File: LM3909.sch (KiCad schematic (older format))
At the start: 18 parts, among them Q1 BC847, Q2A1 BC807, Q2B1 BC807, Q3 BC847, Q4 BC847

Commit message: add pins to schematic
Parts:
- added J? (x2): Conn_01x04, symbol Conn_01x04
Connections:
- net at BT1.1 (+), Q2A1.2 (E), Q2B1.2 (E)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: now also J?.1 (Pin_1)
- net at D1.2 (A), R1.2: now also J?.2 (Pin_2)
- net at C1.1, Q3.3 (C), R5.2: now also J?.2 (Pin_2)
- net at C1.2, D1.1 (K), R2.1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: now also J?.4 (Pin_4)
- net at BT1.2 (-), Q3.2 (E), R3.2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: now also J?.4 (Pin_4)
- net at R2.2, R3.1: now also J?.1 (Pin_1)
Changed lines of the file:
@@
 	5650 1500 6050 1500
+Wire Wire Line
+	6050 1500 6400 1500
 Wire Wire Line
 	3000 1500 3000 1600
@@
 	3000 1950 3000 2000
 Wire Wire Line
-	2400 1900 2400 2000
+	2400 1900 2400 1950
+Wire Wire Line
+	2400 1950 2400 2000
 Wire Wire Line
 	2400 2300 2400 2400
 Wire Wire Line
-	2400 2400 2400 3050
+	2400 2400 2400 2500
+Wire Wire Line
+	2400 2500 2400 3050
 Wire Wire Line
 	2400 3050 2400 3200
@@
 	3000 2300 3000 2400
 Wire Wire Line
-	3000 2400 3000 3150
+	3000 2400 3000 2650
+Wire Wire Line
+	3000 2650 3000 3150
 Wire Wire Line
 	3000 1950 3400 1950
@@
 Connection ~ 2400 3050
 Wire Wire Line
-	2400 3500 2400 3600
+	2400 3500 2400 3550
+Wire Wire Line
+	2400 3550 2400 3600
 Wire Wire Line
 	2400 3900 2400 4000
+Wire Wire Line
+	1800 4000 2400 4000
 Wire Wire Line
 	2400 4000 3000 4000
@@
 	5650 3350 5650 3050
 Wire Wire Line
-	4750 2250 4750 2150
+	4750 2050 4750 2150
 Wire Wire Line
-	4750 2150 4750 2050
+	4750 2150 4750 2250
 Wire Wire Line
 	5200 2150 4750 2150
 Connection ~ 4750 2150
+$Comp
+L Conn_01x04 J?
+U 1 1 5A21951D
+P 6950 2400
+F 0 "J?" H 6950 2600 50  0000 C CNN
+F 1 "Conn_01x04" H 6950 2100 50  0000 C CNN
+F 2 "" H 6950 2400 50  0001 C CNN
+F 3 "" H 6950 2400 50  0001 C CNN
+	1    6950 2400
+	1    0    0    1
+$EndComp
+$Comp
+L Conn_01x04 J?
+U 1 1 5A21958D
+P 1500 2200
+F 0 "J?" H 1500 2400 50  0000 C CNN
+F 1 "Conn_01x04" H 1500 1900 50  0000 C CNN
+F 2 "" H 1500 2200 50  0001 C CNN
+F 3 "" H 1500 2200 50  0001 C CNN
+	1    1500 2200
+	-1   0    0    -1
+$EndComp
+Wire Wire Line
+	1700 2100 2100 2100
+Wire Wire Line
+	2100 2100 2100 3550
+Wire Wire Line
+	2100 3550 2400 3550
+Connection ~ 2400 3550
+Wire Wire Line
+	1700 2200 1950 2200
+Wire Wire Line
+	1950 2200 1950 2650
+Wire Wire Line
+	1950 2650 3000 2650
+Connection ~ 3000 2650
+Wire Wire Line
+	1700 2400 1800 2400
+Wire Wire Line
+	1800 2400 1800 4000
+Connection ~ 2400 4000
+Wire Wire Line
+	6750 2500 6400 2500
+Wire Wire Line
+	6400 2500 6400 1500
+Connection ~ 6050 1500
+Wire Wire Line
+	6750 2200 6650 2200
+Wire Wire Line
+	6650 2200 6650 4100
+Wire Wire Line
+	6650 4100 2250 4100
+Wire Wire Line
+	2250 4100 2250 2500
+Wire Wire Line
+	2250 2500 2400 2500
+Connection ~ 2400 2500
+Wire Wire Line
+	6750 2400 6500 2400
+Wire Wire Line
+	6500 2400 6500 1300
+Wire Wire Line
+	6500 1300 2200 1300
+Wire Wire Line
+	2200 1300 2200 1950
+Wire Wire Line
+	2200 1950 2400 1950
+Connection ~ 2400 1950
 $EndSCHEMATC

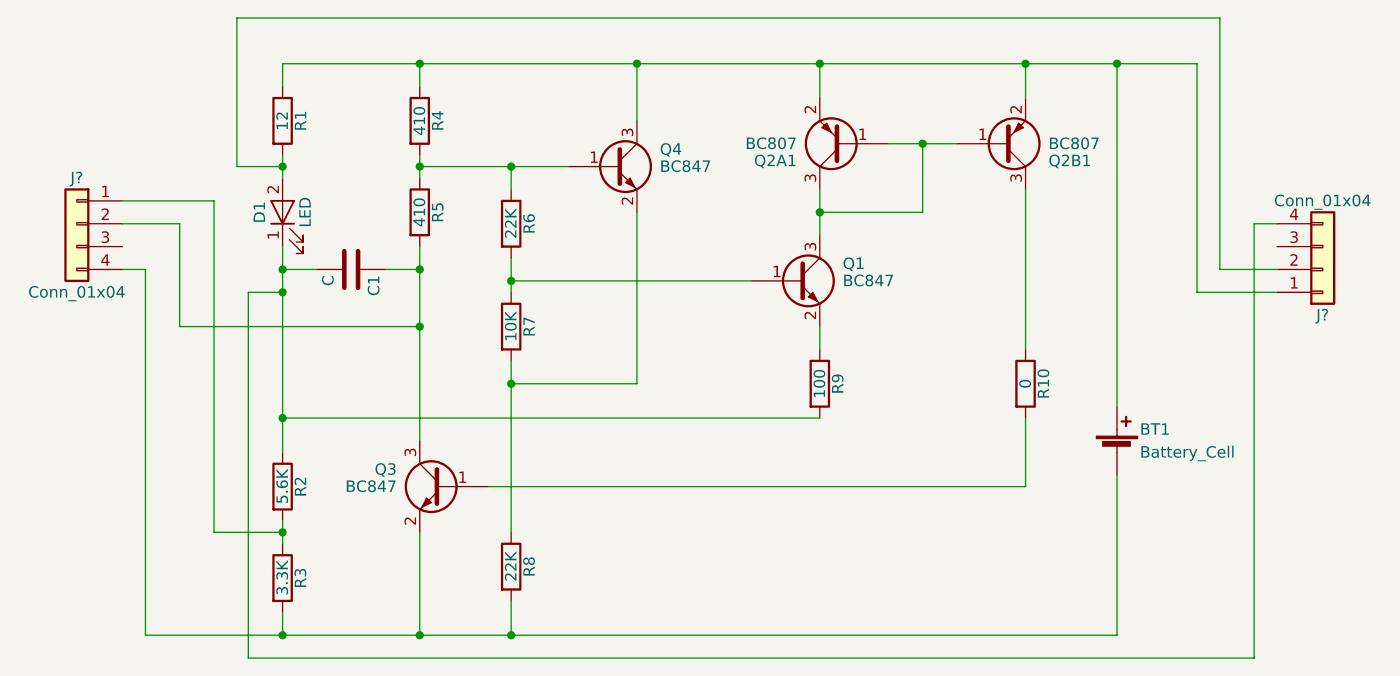
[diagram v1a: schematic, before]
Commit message: add through hole pin footprint
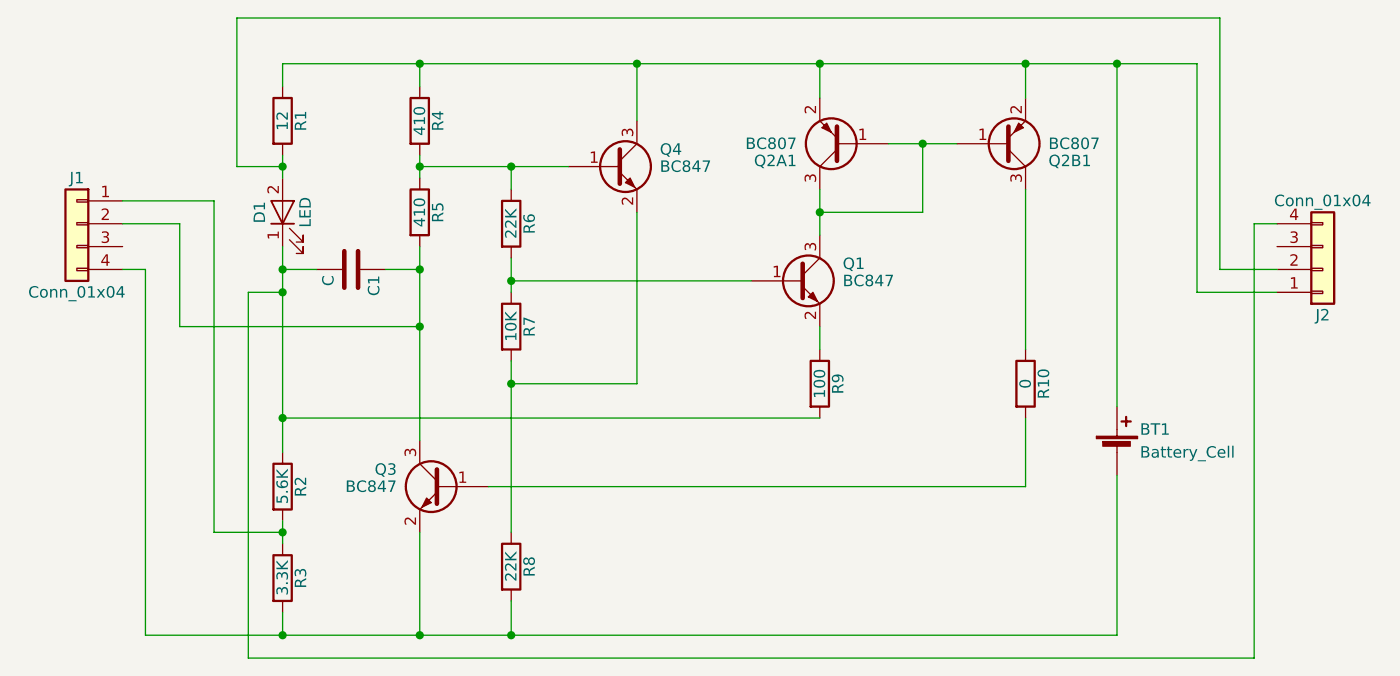
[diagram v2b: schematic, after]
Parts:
- J1, J2: renamed from J?; footprint (none) -> Pin_Headers:Pin_Header_Straight_1x04_Pitch2.54mm
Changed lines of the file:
@@
 	2400 1500 2400 1600
 Wire Wire Line
-	2400 1500 3000 1500
-Wire Wire Line
-	3000 1500 3950 1500
-Wire Wire Line
-	3950 1500 4750 1500
-Wire Wire Line
-	4750 1500 5650 1500
-Wire Wire Line
-	5650 1500 6050 1500
-Wire Wire Line
-	6050 1500 6400 1500
+	2400 1500 6400 1500
 Wire Wire Line
 	3000 1500 3000 1600
 Wire Wire Line
-	3000 1900 3000 1950
+	3000 1900 3000 2000
 Wire Wire Line
-	3000 1950 3000 2000
+	2400 1900 2400 2000
 Wire Wire Line
-	2400 1900 2400 1950
-Wire Wire Line
-	2400 1950 2400 2000
-Wire Wire Line
-	2400 2300 2400 2400
-Wire Wire Line
-	2400 2400 2400 2500
-Wire Wire Line
-	2400 2500 2400 3050
-Wire Wire Line
-	2400 3050 2400 3200
+	2400 2300 2400 3200
 Wire Wire Line
 	2400 2400 2550 2400
@@
 	2850 2400 3000 2400
 Wire Wire Line
-	3000 2300 3000 2400
+	3000 2300 3000 3150
 Wire Wire Line
-	3000 2400 3000 2650
-Wire Wire Line
-	3000 2650 3000 3150
-Wire Wire Line
-	3000 1950 3400 1950
-Wire Wire Line
-	3400 1950 3650 1950
+	3000 1950 3650 1950
 Connection ~ 3000 1950
 Wire Wire Line
@@
 Connection ~ 3400 1950
 Wire Wire Line
-	3400 2350 3400 2450
+	3400 2350 3400 2500
 Wire Wire Line
-	3400 2450 3400 2500
-Wire Wire Line
-	3400 2800 3400 2900
-Wire Wire Line
-	3400 2900 3400 3550
+	3400 2800 3400 3550
 Wire Wire Line
 	3400 2900 3950 2900
@@
 Connection ~ 2400 3050
 Wire Wire Line
-	2400 3500 2400 3550
-Wire Wire Line
-	2400 3550 2400 3600
+	2400 3500 2400 3600
 Wire Wire Line
 	2400 3900 2400 4000
 Wire Wire Line
-	1800 4000 2400 4000
-Wire Wire Line
-	2400 4000 3000 4000
-Wire Wire Line
-	3000 4000 3400 4000
-Wire Wire Line
-	3400 4000 6050 4000
+	1800 4000 6050 4000
 Wire Wire Line
 	3000 4000 3000 3550
@@
 Connection ~ 3400 2900
 Wire Wire Line
-	5050 1850 5200 1850
-Wire Wire Line
-	5200 1850 5350 1850
+	5050 1850 5350 1850
 Wire Wire Line
 	3950 1500 3950 1750
@@
 	5650 3350 5650 3050
 Wire Wire Line
-	4750 2050 4750 2150
-Wire Wire Line
-	4750 2150 4750 2250
+	4750 2050 4750 2250
 Wire Wire Line
 	5200 2150 4750 2150
 Connection ~ 4750 2150
 $Comp
-L Conn_01x04 J?
+L Conn_01x04 J2
 U 1 1 5A21951D
 P 6950 2400
-F 0 "J?" H 6950 2600 50  0000 C CNN
+F 0 "J2" H 6950 2600 50  0000 C CNN
 F 1 "Conn_01x04" H 6950 2100 50  0000 C CNN
-F 2 "" H 6950 2400 50  0001 C CNN
+F 2 "Pin_Headers:Pin_Header_Straight_1x04_Pitch2.54mm" H 6950 2400 50  0001 C CNN
 F 3 "" H 6950 2400 50  0001 C CNN
 	1    6950 2400
@@
 $EndComp
 $Comp
-L Conn_01x04 J?
+L Conn_01x04 J1
 U 1 1 5A21958D
 P 1500 2200
-F 0 "J?" H 1500 2400 50  0000 C CNN
+F 0 "J1" H 1500 2400 50  0000 C CNN
 F 1 "Conn_01x04" H 1500 1900 50  0000 C CNN
-F 2 "" H 1500 2200 50  0001 C CNN
+F 2 "Pin_Headers:Pin_Header_Straight_1x04_Pitch2.54mm" H 1500 2200 50  0001 C CNN
 F 3 "" H 1500 2200 50  0001 C CNN
 	1    1500 2200

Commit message: replace BC8*7 with MMBT390* transistors
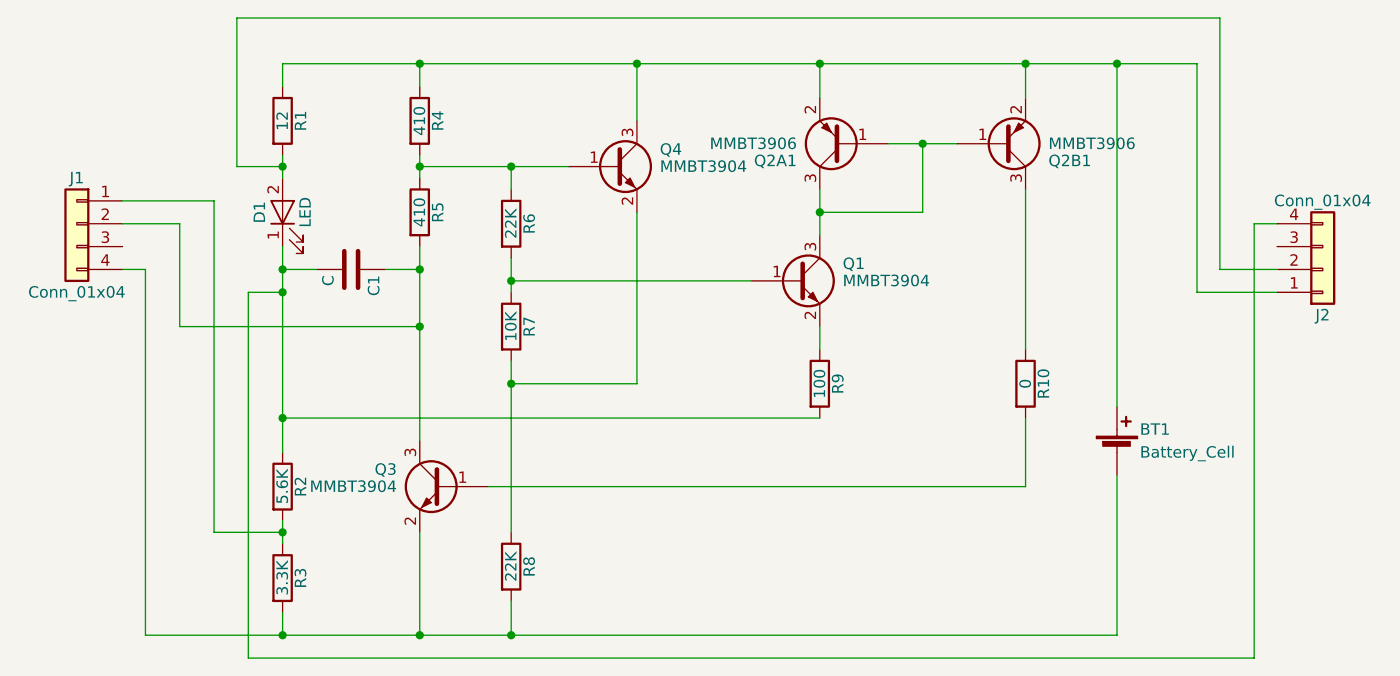
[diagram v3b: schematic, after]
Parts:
- removed Q1, Q3, Q4: BC847, TO_SOT_Packages_SMD:SOT-23, symbol BC847
- removed Q2A1, Q2B1: BC807, TO_SOT_Packages_SMD:SOT-23, symbol BC807
- added Q1, Q3, Q4: MMBT3904, TO_SOT_Packages_SMD:SOT-23, symbol MMBT3904
- added Q2A1, Q2B1: MMBT3906, TO_SOT_Packages_SMD:SOT-23, symbol MMBT3906
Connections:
- net at BT1.1 (+), J2.1 (Pin_1), R1.1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: now also Q2A1.2 (E), Q2B1.2 (E), Q4.3 (C)
- net at R4.2, R5.1, R6.1: now also Q4.1 (B)
- net at C1.1, J1.2 (Pin_2), R5.2: now also Q3.3 (C)
- net at R9.1: now also Q1.2 (E)
- net at R7.2, R8.1: now also Q4.2 (E)
- net at BT1.2 (-), J1.4 (Pin_4), R3.2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: now also Q3.2 (E)
- net at R6.2, R7.1: now also Q1.1 (B)
- net at R10.2: now also Q3.1 (B)
- net at R10.1: now also Q2B1.3 (C)
- new net: Q1.3 (C), Q2A1.1 (B), Q2A1.3 (C), Q2B1.1 (B)
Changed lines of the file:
@@
-$EndComp
-$Comp
-L BC847 Q4
-U 1 1 5A204D01
-P 3850 1950
-F 0 "Q4" H 4050 2025 50  0000 L CNN
-F 1 "BC847" H 4050 1950 50  0000 L CNN
-F 2 "TO_SOT_Packages_SMD:SOT-23" H 4050 1875 50  0001 L CIN
-F 3 "" H 3850 1950 50  0001 L CNN
-	1    3850 1950
-	1    0    0    -1
-$EndComp
-$Comp
-L BC847 Q1
-U 1 1 5A2054C7
-P 4650 2450
-F 0 "Q1" H 4850 2525 50  0000 L CNN
-F 1 "BC847" H 4850 2450 50  0000 L CNN
-F 2 "TO_SOT_Packages_SMD:SOT-23" H 4850 2375 50  0001 L CIN
-F 3 "" H 4650 2450 50  0001 L CNN
-	1    4650 2450
-	1    0    0    -1
-$EndComp
-$Comp
-L BC847 Q3
-U 1 1 5A205527
-P 3100 3350
-F 0 "Q3" H 3300 3425 50  0000 L CNN
-F 1 "BC847" H 3300 3350 50  0000 L CNN
-F 2 "TO_SOT_Packages_SMD:SOT-23" H 3300 3275 50  0001 L CIN
-F 3 "" H 3100 3350 50  0001 L CNN
-	1    3100 3350
-	-1   0    0    -1
-$EndComp
-$Comp
-L BC807 Q2B1
-U 1 1 5A205CDD
-P 5550 1850
-F 0 "Q2B1" H 5750 1925 50  0000 L CNN
-F 1 "BC807" H 5750 1850 50  0000 L CNN
-F 2 "TO_SOT_Packages_SMD:SOT-23" H 5750 1775 50  0001 L CIN
-F 3 "" H 5550 1850 50  0001 L CNN
-	1    5550 1850
-	1    0    0    1
-$EndComp
-$Comp
-L BC807 Q2A1
-U 1 1 5A205D5E
-P 4850 1850
-F 0 "Q2A1" H 5050 1925 50  0000 L CNN
-F 1 "BC807" H 5050 1850 50  0000 L CNN
-F 2 "TO_SOT_Packages_SMD:SOT-23" H 5050 1775 50  0001 L CIN
-F 3 "" H 4850 1850 50  0001 L CNN
-	1    4850 1850
-	-1   0    0    1
 $EndComp
 $Comp
@@
 	2200 1950 2400 1950
 Connection ~ 2400 1950
+$Comp
+L MMBT3904 Q4
+U 1 1 5A256999
+P 3850 1950
+F 0 "Q4" H 4050 2025 50  0000 L CNN
+F 1 "MMBT3904" H 4050 1950 50  0000 L CNN
+F 2 "TO_SOT_Packages_SMD:SOT-23" H 4050 1875 50  0001 L CIN
+F 3 "" H 3850 1950 50  0001 L CNN
+	1    3850 1950
+	1    0    0    -1
+$EndComp
+$Comp
+L MMBT3904 Q1
+U 1 1 5A256DC3
+P 4650 2450
+F 0 "Q1" H 4850 2525 50  0000 L CNN
+F 1 "MMBT3904" H 4850 2450 50  0000 L CNN
+F 2 "TO_SOT_Packages_SMD:SOT-23" H 4850 2375 50  0001 L CIN
+F 3 "" H 4650 2450 50  0001 L CNN
+	1    4650 2450
+	1    0    0    -1
+$EndComp
+$Comp
+L MMBT3904 Q3
+U 1 1 5A256E35
+P 3100 3350
+F 0 "Q3" H 3300 3425 50  0000 L CNN
+F 1 "MMBT3904" H 3300 3350 50  0000 L CNN
+F 2 "TO_SOT_Packages_SMD:SOT-23" H 3300 3275 50  0001 L CIN
+F 3 "" H 3100 3350 50  0001 L CNN
+	1    3100 3350
+	-1   0    0    -1
+$EndComp
+$Comp
+L MMBT3906 Q2A1
+U 1 1 5A2571F4
+P 4850 1850
+F 0 "Q2A1" H 5050 1925 50  0000 L CNN
+F 1 "MMBT3906" H 5050 1850 50  0000 L CNN
+F 2 "TO_SOT_Packages_SMD:SOT-23" H 5050 1775 50  0001 L CIN
+F 3 "" H 4850 1850 50  0001 L CNN
+	1    4850 1850
+	-1   0    0    1
+$EndComp
+$Comp
+L MMBT3906 Q2B1
+U 1 1 5A25759B
+P 5550 1850
+F 0 "Q2B1" H 5750 1925 50  0000 L CNN
+F 1 "MMBT3906" H 5750 1850 50  0000 L CNN
+F 2 "TO_SOT_Packages_SMD:SOT-23" H 5750 1775 50  0001 L CIN
+F 3 "" H 5550 1850 50  0001 L CNN
+	1    5550 1850
+	1    0    0    1
+$EndComp
 $EndSCHEMATC
